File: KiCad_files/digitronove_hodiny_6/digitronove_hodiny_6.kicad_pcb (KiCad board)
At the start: 2 copper layers, 54 parts, among them J1 Nixie_CATHODES, J2 Nixie_ANODES, J3 Conn_01x05, J4 Conn_01x05, J5 Conn_01x02, Q1 MPSA42, Q10 MPSA42, Q2 MPSA42, Q3 MPSA42, Q4 MPSA42, Q5 MPSA42, Q6 MPSA42, Q7 MPSA42, Q8 MPSA42, Q9 MPSA42, U1 WeMos_D1_mini, U10 74HC595, U12 AMS1117-3.3, U2 74HC595, U3 74HC595, U4 TLP627, U5 TLP627, U6 TLP627, U7 TLP627, U8 TLP627, U9 TLP627

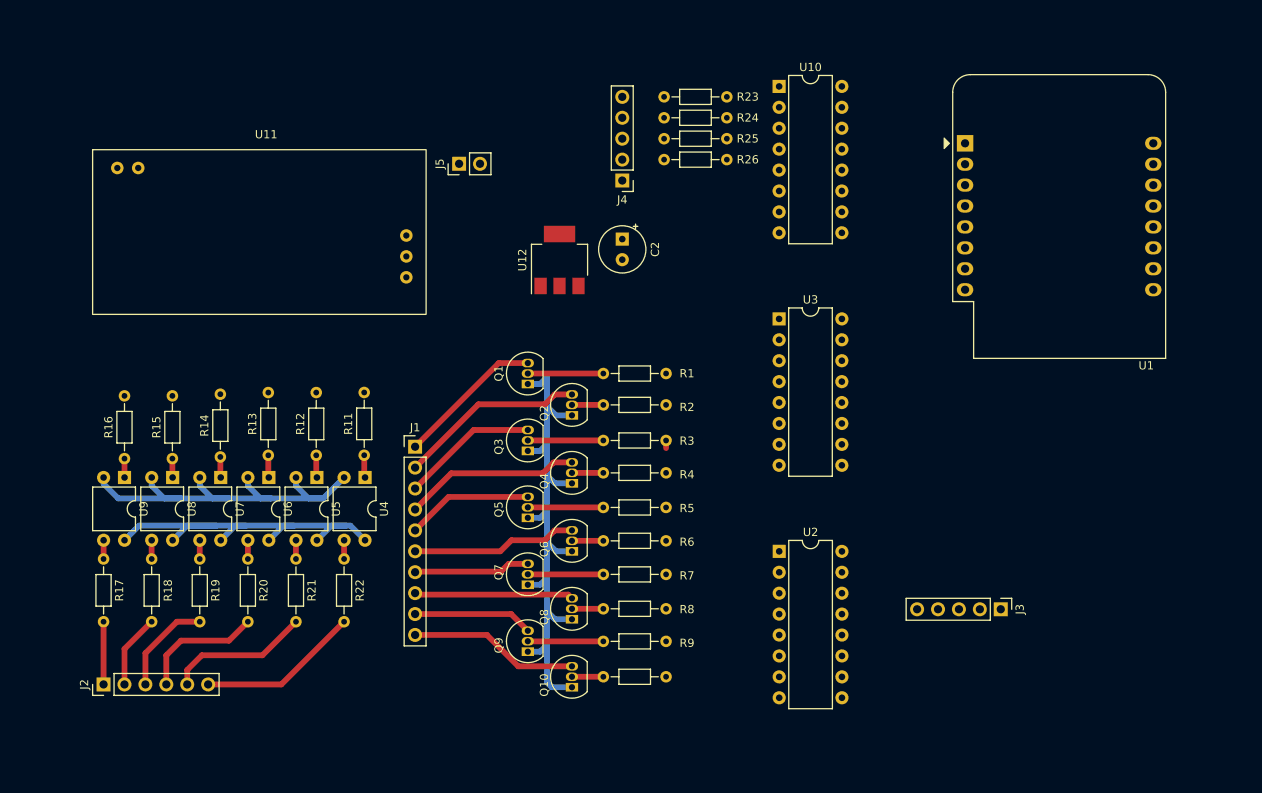
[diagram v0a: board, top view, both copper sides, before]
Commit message: KiCad PCB and Schema desing update
Nearly finished PCB desing. Changed the schema according to my breadboard prototype.
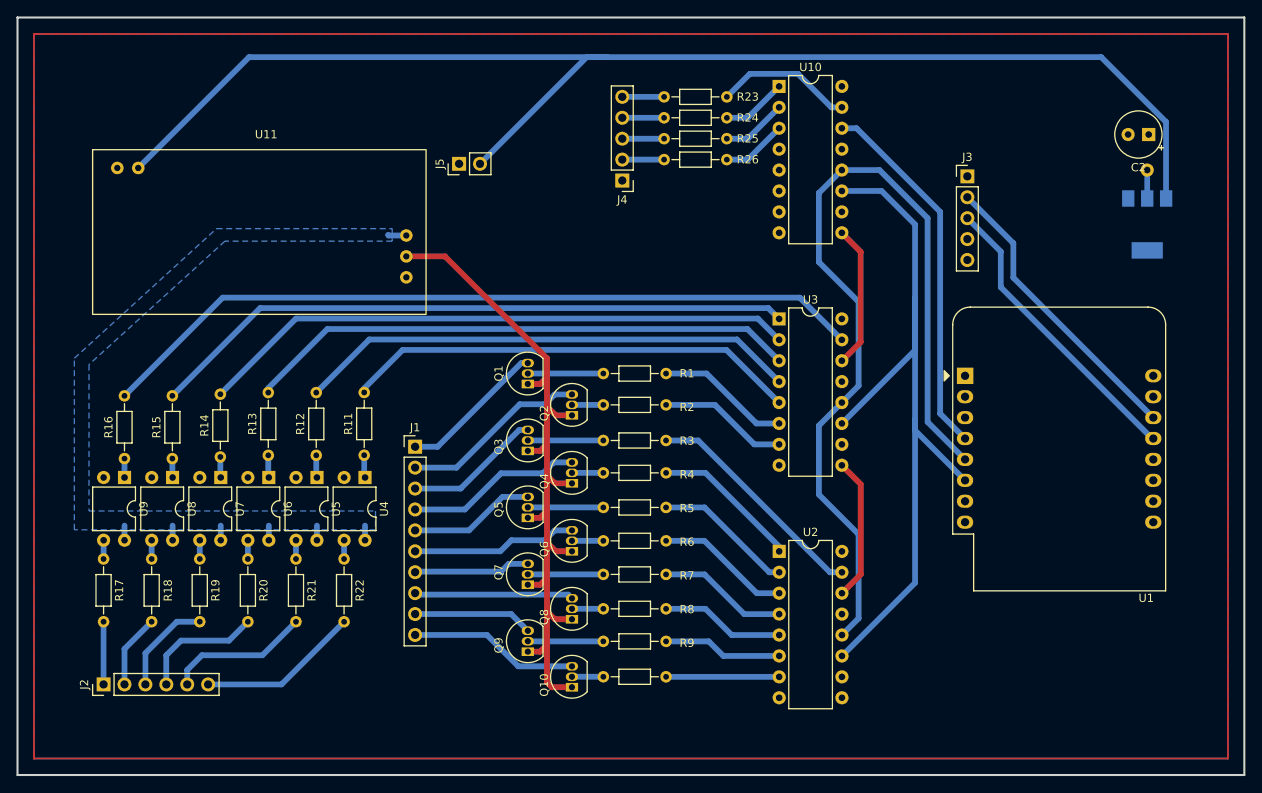
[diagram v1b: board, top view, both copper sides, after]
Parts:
- added ?: , , F.Cu at (235.2, 49.5)
- U12: moved to B.Cu
- moved U12 71.5 mm to (235.2, 56.1), turned to -90 degrees
- moved C2 65.2 mm to (235.4, 45.2), turned to 180 degrees
- moved J3 52.7 mm to (213.4, 50.3), turned to 0 degrees
- moved U1 28.2 mm to (213.1, 74.5)
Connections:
- U1 pad 5: CLOCK -> LATCH
- U1 pad 6: LATCH -> CLOCK
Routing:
- net VCC: track 0.00 -> 163.8 mm
- net LATCH: track 0.00 -> 108.5 mm
- net CLOCK: track 0.00 -> 95.6 mm
- net ANODE_0: track 0.00 -> 94.2 mm
- net ANODE_1: track 0.00 -> 78.6 mm
- net ANODE_2: track 0.00 -> 72.7 mm
- net ANODE_3: track 0.00 -> 67.1 mm
- net ANODE_4: track 0.00 -> 61.0 mm
- net ANODE_5: track 0.00 -> 55.5 mm
- net GND: track 51.6 -> 0.15 mm
- net DATA: track 0.00 -> 44.9 mm
- net SCL: track 0.00 -> 36.2 mm
- net SDA: track 0.00 -> 36.1 mm
- net HV_ANODE: track 48.6 -> 12.9 mm
- net CATHODE_2: track 0.93 -> 28.0 mm
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- added copper zone on F.Cu, net 3V3
- added copper zone on B.Cu, net GND
- added copper zone on B.Cu, net HV_ANODE
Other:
- board outline added: 149 x 92 mm

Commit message: PCB Update
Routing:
- net HV_ANODE: track 12.9 -> 119.0 mm
- net 3V3: track 4.19 -> 5.64 mm
- removed copper zone on B.Cu, net HV_ANODE
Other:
- outline, holes or cut-outs redrawn
- board text added: "Digitronové hodiny Vojtěch Pindur 6.2.2024 ver:0.1"
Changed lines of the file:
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@@
       (net 83 "3V3") (pinfunction "VO") (pintype "power_out"))
     (pad "2" smd rect (at 3.15 0 270) (size 2 3.8) (layers "B.Cu" "B.Paste" "B.Mask")
-      (pinfunction "VO") (pintype "power_out"))
+      (net 83 "3V3") (pinfunction "VO") (pintype "power_out"))
     (pad "3" smd rect (at -3.15 -2.3 270) (size 2 1.5) (layers "B.Cu" "B.Paste" "B.Mask")
       (net 44 "VCC") (pinfunction "VI") (pintype "power_in"))
@@
   (gr_rect (start 104 37) (end 241 117)
     (stroke (width 0.2) (type default)) (fill none) (layer "Dwgs.User"))
+  (gr_circle (center 241 117) (end 244 117)
+    (stroke (width 0.25) (type default)) (fill none) (layer "Edge.Cuts"))
+  (gr_circle (center 241 37) (end 244 37)
+    (stroke (width 0.25) (type default)) (fill none) (layer "Edge.Cuts"))
   (gr_rect (start 98 31) (end 247 123)
     (stroke (width 0.25) (type default)) (fill none) (layer "Edge.Cuts"))
+  (gr_circle (center 104 117) (end 107 117)
+    (stroke (width 0.25) (type default)) (fill none) (layer "Edge.Cuts"))
+  (gr_circle (center 104 37) (end 107 37)
+    (stroke (width 0.25) (type default)) (fill none) (layer "Edge.Cuts"))
+  (gr_text "Digitronové hodiny\nVojtěch Pindur\n6.2.2024  ver:0.1" (at 215.138 114.554) (layer "F.Cu")
+    (effects (font (size 1.5 1.5) (thickness 0.3) bold) (justify left bottom))
+  )
   (segment (start 159.186 72.97) (end 149.026 83.13) (width 0.7) (layer "B.Cu") (net 1))
   (segment (start 159.980356 72.97) (end 159.186 72.97) (width 0.7) (layer "B.Cu") (net 1))
@@
   (segment (start 192.999 65.024) (end 122.921 65.024) (width 0.7) (layer "B.Cu") (net 34))
   (segment (start 122.921 65.024) (end 110.993 76.952) (width 0.7) (layer "B.Cu") (net 34))
-  (segment (start 140.208 94.488) (end 140.208 92.71) (width 0.7) (layer "B.Cu") (net 35))
-  (segment (start 134.366 94.488) (end 134.366 92.71) (width 0.7) (layer "B.Cu") (net 35))
-  (segment (start 122.682 94.488) (end 122.682 92.71) (width 0.7) (layer "B.Cu") (net 35))
-  (segment (start 116.84 94.488) (end 116.84 92.71) (width 0.7) (layer "B.Cu") (net 35))
-  (segment (start 110.998 94.488) (end 110.998 92.71) (width 0.7) (layer "B.Cu") (net 35))
-  (segment (start 128.524 94.488) (end 128.524 92.71) (width 0.7) (layer "B.Cu") (net 35))
-  (segment (start 145.223 57.476) (end 143.074 57.476) (width 0.7) (layer "B.Cu") (net 35))
-  (segment (start 143.074 57.476) (end 143.002 57.404) (width 0.7) (layer "B.Cu") (net 35))
+  (segment (start 126.492 91.694) (end 125.73 91.694) (width 0.7) (layer "B.Cu") (net 35))
+  (segment (start 109.22 91.694) (end 105.41 91.694) (width 0.7) (layer "B.Cu") (net 35))
+  (segment (start 120.904 91.694) (end 120.396 91.694) (width 0.7) (layer "B.Cu") (net 35))
+  (segment (start 134.366 93.726) (end 132.334 91.694) (width 0.7) (layer "B.Cu") (net 35))
+  (segment (start 140.208 93.726) (end 140.208 94.488) (width 0.7) (layer "B.Cu") (net 35))
+  (segment (start 125.73 91.694) (end 132.334 91.694) (width 0.7) (layer "B.Cu") (net 35))
+  (segment (start 132.334 91.694) (end 138.176 91.694) (width 0.7) (layer "B.Cu") (net 35))
+  (segment (start 123.626 57.476) (end 145.223 57.476) (width 0.7) (layer "B.Cu") (net 35))
+  (segment (start 114.808 91.694) (end 120.396 91.694) (width 0.7) (layer "B.Cu") (net 35))
+  (segment (start 122.682 93.472) (end 120.904 91.694) (width 0.7) (layer "B.Cu") (net 35))
+  (segment (start 110.998 94.488) (end 110.998 93.472) (width 0.7) (layer "B.Cu") (net 35))
+  (segment (start 134.366 94.488) (end 134.366 93.726) (width 0.7) (layer "B.Cu") (net 35))
+  (segment (start 128.524 93.726) (end 126.492 91.694) (width 0.7) (layer "B.Cu") (net 35))
+  (segment (start 116.84 93.726) (end 114.808 91.694) (width 0.7) (layer "B.Cu") (net 35))
+  (segment (start 138.176 91.694) (end 140.208 93.726) (width 0.7) (layer "B.Cu") (net 35))
+  (segment (start 116.84 94.488) (end 116.84 93.726) (width 0.7) (layer "B.Cu") (net 35))
+  (segment (start 114.808 91.694) (end 109.22 91.694) (width 0.7) (layer "B.Cu") (net 35))
+  (segment (start 110.998 93.472) (end 109.22 91.694) (width 0.7) (layer "B.Cu") (net 35))
+  (segment (start 105.41 75.692) (end 123.626 57.476) (width 0.7) (layer "B.Cu") (net 35))
+  (segment (start 105.41 91.694) (end 105.41 75.692) (width 0.7) (layer "B.Cu") (net 35))
+  (segment (start 120.396 91.694) (end 125.73 91.694) (width 0.7) (layer "B.Cu") (net 35))
+  (segment (start 122.682 94.488) (end 122.682 93.472) (width 0.7) (layer "B.Cu") (net 35))
+  (segment (start 128.524 94.488) (end 128.524 93.726) (width 0.7) (layer "B.Cu") (net 35))
   (segment (start 207.01 71.415) (end 207.01 65.024) (width 0.7) (layer "B.Cu") (net 38))
   (segment (start 202.946 52.07) (end 198.12 52.07) (width 0.7) (layer "B.Cu") (net 38))
@@
   (segment (start 213.083 92.295) (end 213.267 92.295) (width 0.7) (layer "F.Cu") (net 83))
   (segment (start 235.204 45.392369) (end 235.384369 45.212) (width 0.7) (layer "F.Cu") (net 83))
+  (segment (start 233.75 49.53) (end 235.204 49.53) (width 0.7) (layer "F.Cu") (net 83))
   (segment (start 235.204 52.984) (end 235.204 49.53) (width 0.7) (layer "B.Cu") (net 83))
   (segment (start 235.943 82.135) (end 235.805 82.135) (width 0.7) (layer "B.Cu") (net 85))
@@
     )
   )
-  (zone (net 35) (net_name "HV_ANODE") (layer "B.Cu") (name "HV_ANODE") (hatch edge 0.5)
-    (priority 2)
-    (connect_pads yes (clearance 1))
-    (min_thickness 0.5) (filled_areas_thickness no)
-    (fill yes (thermal_gap 0.5) (thermal_bridge_width 0.5) (island_removal_mode 1) (island_area_min 10))
+  (zone (net 0) (net_name "") (layer "F.Cu") (name "POPISEK") (hatch edge 0.5)
+    (connect_pads (clearance 0))
+    (min_thickness 0.25) (filled_areas_thickness no)
+    (keepout (tracks not_allowed) (vias not_allowed) (pads not_allowed) (copperpour not_allowed) (footprints allowed))
+    (fill (thermal_gap 0.5) (thermal_bridge_width 0.5))
     (polygon
       (pts
-        (xy 143.51 58.166)
-        (xy 123.19 58.166)
-        (xy 106.68 73.152)
-        (xy 106.68 90.932)
-        (xy 141.478 90.932)
-        (xy 141.478 93.218)
-        (xy 104.902 93.218)
-        (xy 104.902 72.39)
-        (xy 122.174 56.642)
-        (xy 143.51 56.642)
+        (xy 210.82 105.156)
+        (xy 241.046 105.156)
+        (xy 241.046 117.094)
+        (xy 210.82 117.094)
       )
     )

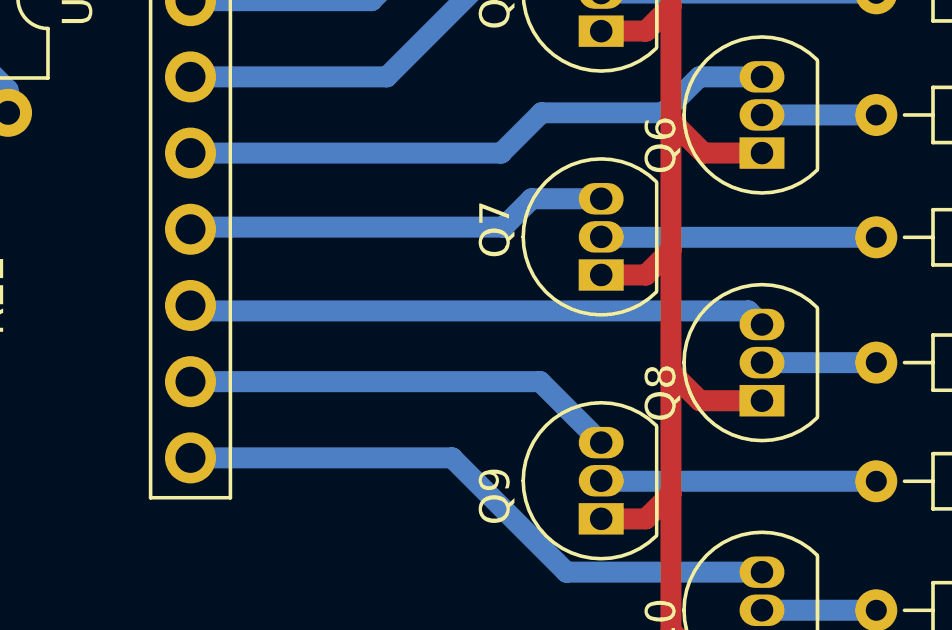
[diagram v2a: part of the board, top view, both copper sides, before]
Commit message: General changes.
Removed some unnecesary files, minor changes to PCB design, added  a 3D Model directory for future files.
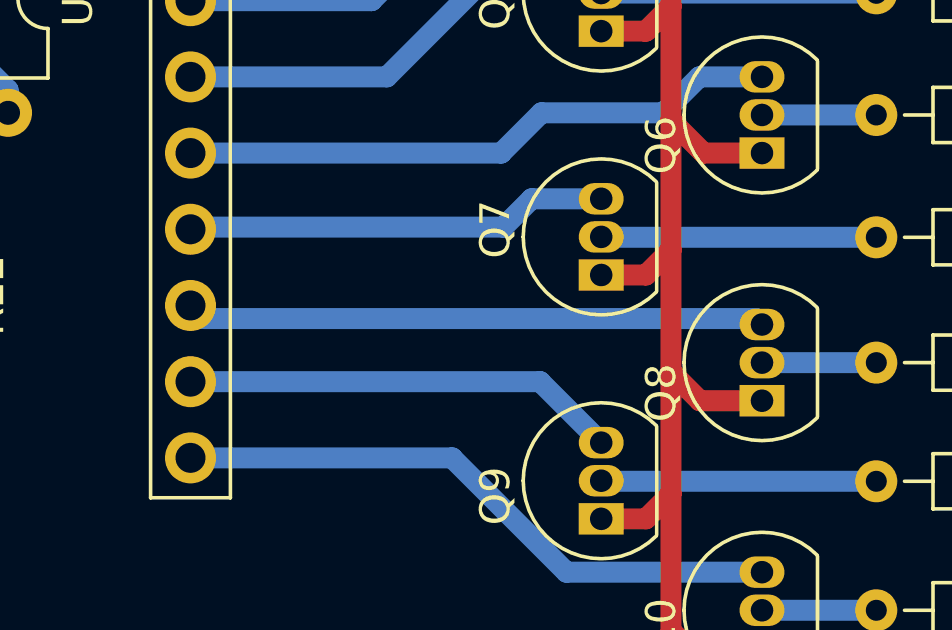
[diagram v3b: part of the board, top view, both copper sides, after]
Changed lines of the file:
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@@
       (net 83 "3V3") (pinfunction "VO") (pintype "power_out"))
     (pad "2" smd rect (at 3.15 0 270) (size 2 3.8) (layers "B.Cu" "B.Paste" "B.Mask")
-      (net 83 "3V3") (pinfunction "VO") (pintype "power_out"))
+      (pinfunction "VO") (pintype "power_out"))
     (pad "3" smd rect (at -3.15 -2.3 270) (size 2 1.5) (layers "B.Cu" "B.Paste" "B.Mask")
       (net 44 "VCC") (pinfunction "VI") (pintype "power_in"))
@@
     (stroke (width 0.25) (type default)) (fill none) (layer "Edge.Cuts"))
   (gr_circle (center 104 37) (end 107 37)
-    (stroke (width 0.25) (type default)) (fill none) (layer "Edge.Cuts"))
-  (gr_text "Digitronové hodiny\nVojtěch Pindur\n6.2.2024  ver:0.1" (at 215.138 114.554) (layer "F.Cu")
+    (stroke (width 0.25) (type solid)) (fill none) (layer "Edge.Cuts"))
+  (gr_text "Digitronové hodiny\nVojtěch Pindur\n6.2.2024  ver:0.1" (at 215.138 114.554) (layer "F.Cu" knockout)
     (effects (font (size 1.5 1.5) (thickness 0.3) bold) (justify left bottom))
   )
@@
   (segment (start 159.980356 97.354) (end 157.662 97.354) (width 0.7) (layer "B.Cu") (net 7))
   (segment (start 157.662 97.354) (end 156.718 98.298) (width 0.7) (layer "B.Cu") (net 7))
-  (segment (start 164.887 101.092) (end 165.34 101.545) (width 0.7) (layer "B.Cu") (net 8))
-  (segment (start 146.29 100.91) (end 146.472 101.092) (width 0.7) (layer "B.Cu") (net 8))
-  (segment (start 146.472 101.092) (end 164.887 101.092) (width 0.7) (layer "B.Cu") (net 8))
+  (segment (start 146.29 100.91) (end 146.726 101.346) (width 0.7) (layer "B.Cu") (net 8))
+  (segment (start 165.141 101.346) (end 165.34 101.545) (width 0.7) (layer "B.Cu") (net 8))
+  (segment (start 146.726 101.346) (end 165.141 101.346) (width 0.7) (layer "B.Cu") (net 8))
   (segment (start 146.29 103.45) (end 157.948356 103.45) (width 0.7) (layer "B.Cu") (net 9))
   (segment (start 157.948356 103.45) (end 159.980356 105.482) (width 0.7) (layer "B.Cu") (net 9))
@@
     (connect_pads yes (clearance 1))
     (min_thickness 0.5) (filled_areas_thickness no)
-    (fill yes (thermal_gap 0.5) (thermal_bridge_width 0.5) (island_removal_mode 1) (island_area_min 10))
+    (fill yes (thermal_gap 0.5) (thermal_bridge_width 0.5))
     (polygon
       (pts
@@
       )
     )
-  )
-  (zone (net 0) (net_name "") (layer "F.Cu") (name "POPISEK") (hatch edge 0.5)
-    (connect_pads (clearance 0))
-    (min_thickness 0.25) (filled_areas_thickness no)
-    (keepout (tracks not_allowed) (vias not_allowed) (pads not_allowed) (copperpour not_allowed) (footprints allowed))
-    (fill (thermal_gap 0.5) (thermal_bridge_width 0.5))
-    (polygon
-      (pts
-        (xy 210.82 105.156)
-        (xy 241.046 105.156)
-        (xy 241.046 117.094)
-        (xy 210.82 117.094)
-      )
-    )
-  )
-  (zone (net 0) (net_name "") (layer "B.Cu") (name "3V3") (hatch edge 0.5)
-    (connect_pads (clearance 0))
-    (min_thickness 0.5) (filled_areas_thickness no)
-    (keepout (tracks not_allowed) (vias not_allowed) (pads not_allowed) (copperpour not_allowed) (footprints allowed))
-    (fill (thermal_gap 0.5) (thermal_bridge_width 0.5) (island_removal_mode 1) (island_area_min 10))
-    (polygon
-      (pts
-        (xy 191.783312 66.413241)
-        (xy 191.7897 74.946841)
-        (xy 197.0997 74.946841)
-        (xy 197.093312 70.613241)
-      )
-    )
-  )
-  (zone (net 0) (net_name "") (layer "B.Cu") (name "3V3") (hatch edge 0.5)
-    (connect_pads (clearance 0))
-    (min_thickness 0.5) (filled_areas_thickness no)
-    (keepout (tracks not_allowed) (vias not_allowed) (pads not_allowed) (copperpour not_allowed) (footprints allowed))
-    (fill (thermal_gap 0.5) (thermal_bridge_width 0.5) (island_removal_mode 1) (island_area_min 10))
-    (polygon
-      (pts
-        (xy 191.75 95.432)
-        (xy 191.756388 103.2036)
-        (xy 197.066388 103.2036)
-        (xy 197.06 99.632)
-      )
-    )
